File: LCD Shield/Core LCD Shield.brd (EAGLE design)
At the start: 38.1 x 35.6 mm, 8 parts, among them IC1 MC33269T-5.0, J1 TWIG_2.0-DIP-FEMALE

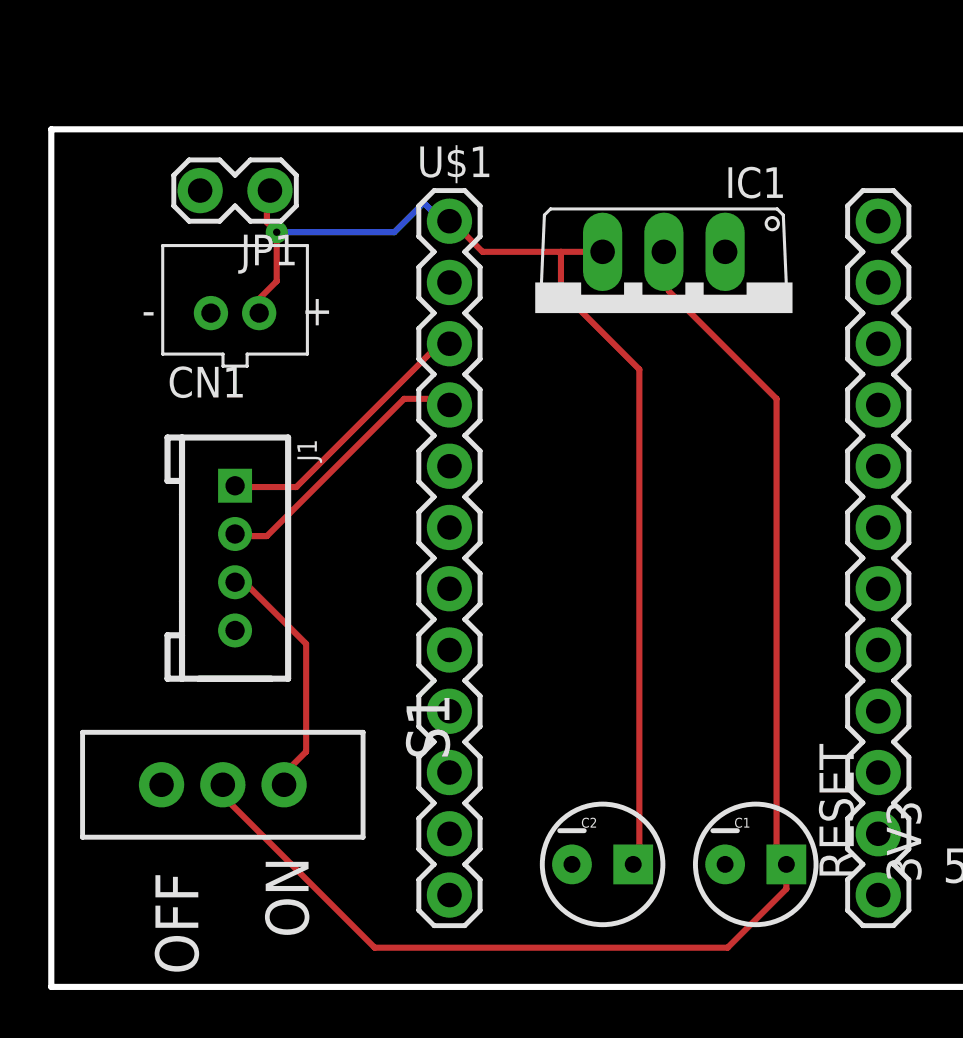
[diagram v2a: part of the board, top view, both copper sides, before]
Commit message: Reviewed LCD Shield
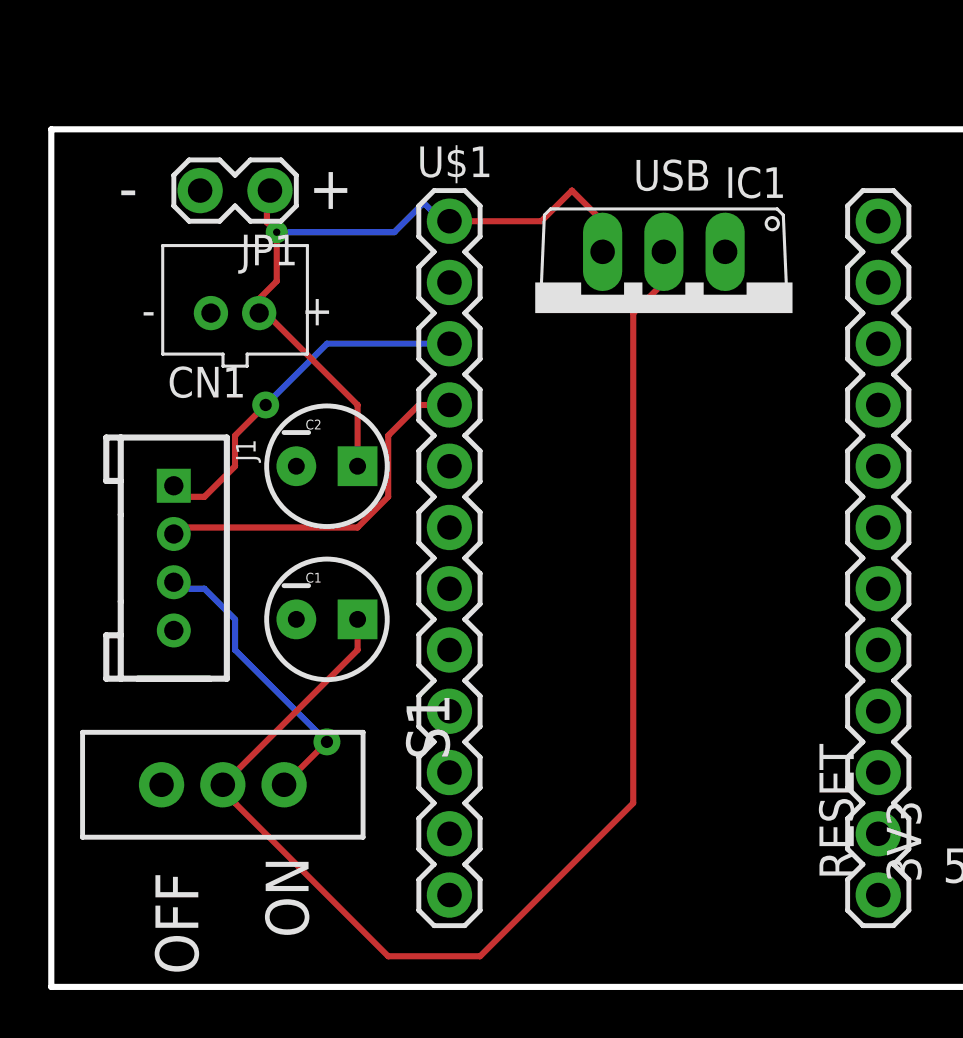
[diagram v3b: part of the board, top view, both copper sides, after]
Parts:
- added U$2: (no value), Spark:SPARK_LOGO
- moved C1 20.5 mm to (11.4, 15.2)
- moved C2 20.1 mm to (11.4, 21.6)
- moved J1 2.54 mm to (5.08, 17.8)
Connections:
- net +3V3 renamed VCC
- removed net RESET: U$1.23
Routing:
- net VIN: track 47.4 -> 30.6 mm
- net RX: track 11.4 -> 15.3 mm
- net TX: track 11.5 -> 15.3 mm, vias 0 -> 1
- net +5V: track 10.5 -> 12.5 mm, vias 0 -> 1
- net N1: track 56.1 -> 55.2 mm
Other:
- board text added: "+"
- board text added: "-"
- board text added: "Spark LCD Shield v0.1 2013-04-08"
- board text added: "USB"
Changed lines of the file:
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@@
 <wire x1="38.1" y1="35.56" x2="38.1" y2="0" width="0.254" layer="20"/>
 <wire x1="38.1" y1="0" x2="0" y2="0" width="0.254" layer="20"/>
+<text x="10.668" y="32.258" size="1.778" layer="21" font="vector" ratio="15">+</text>
+<text x="2.794" y="32.258" size="1.778" layer="21" font="vector" ratio="15">-</text>
+<text x="24.13" y="33.02" size="1.27" layer="21" font="vector" ratio="15">USB</text>
+<text x="22.86" y="2.54" size="1.27" layer="22" font="vector" ratio="15" rot="MR90">Spark LCD Shield
+v0.1
+2013-04-08</text>
 </plain>
 <attributes>
@@
 <element name="U$1" library="Spark" package="SPARK_CORE" value="SPARK_CORECORE" x="25.4" y="17.78"/>
 <element name="IC1" library="linear" package="TO220V" value="MC33269T-5.0" x="25.4" y="27.94" rot="R180"/>
-<element name="C1" library="SparkFun-Capacitors" package="CPOL-RADIAL-10UF-25V" value="10uF" x="29.21" y="5.08"/>
-<element name="C2" library="SparkFun-Capacitors" package="CPOL-RADIAL-10UF-25V" value="1uF" x="22.86" y="5.08"/>
+<element name="C1" library="SparkFun-Capacitors" package="CPOL-RADIAL-10UF-25V" value="10uF" x="11.43" y="15.24"/>
+<element name="C2" library="SparkFun-Capacitors" package="CPOL-RADIAL-10UF-25V" value="1uF" x="11.43" y="21.59"/>
 <element name="CN1" library="adafruit" package="JST-PH-2-THM" value="" x="7.62" y="27.94"/>
 <element name="JP1" library="SparkFun-Connectors" package="1X02_LOCK" value="" x="8.89" y="33.02" rot="R180"/>
 <element name="S1" library="SparkFun-Electromechanical" package="SWITCH-SPDT" value="" x="7.112" y="8.382" rot="R270"/>
-<element name="J1" library="Connector" package="2.0_1X4" value="TWIG_2.0-DIP-FEMALE" x="7.62" y="17.78" rot="R270"/>
+<element name="J1" library="Connector" package="2.0_1X4" value="TWIG_2.0-DIP-FEMALE" x="5.08" y="17.78" rot="R270"/>
+<element name="U$2" library="Spark" package="SPARK_LOGO" value="" x="22.86" y="2.54"/>
 </elements>
 <signals>
@@
 <contactref element="S1" pad="1"/>
 <contactref element="J1" pad="3"/>
-<wire x1="8.128" y1="16.6624" x2="7.7216" y2="16.6624" width="0.254" layer="1"/>
-<wire x1="10.5664" y1="14.224" x2="8.128" y2="16.6624" width="0.254" layer="1"/>
-<wire x1="10.5664" y1="9.7536" x2="10.5664" y2="14.224" width="0.254" layer="1"/>
-<wire x1="9.3472" y1="8.5344" x2="10.5664" y2="9.7536" width="0.254" layer="1"/>
-<wire x1="7.7216" y1="16.6624" x2="7.62" y2="16.78" width="0.254" layer="1"/>
-<wire x1="9.3472" y1="8.5344" x2="9.652" y2="8.382" width="0.254" layer="1"/>
+<wire x1="11.43" y1="10.16" x2="9.652" y2="8.382" width="0.254" layer="1"/>
+<wire x1="7.62" y1="13.97" x2="11.43" y2="10.16" width="0.254" layer="16"/>
+<wire x1="7.62" y1="15.24" x2="7.62" y2="13.97" width="0.254" layer="16"/>
+<wire x1="6.35" y1="16.51" x2="7.62" y2="15.24" width="0.254" layer="16"/>
+<wire x1="5.08" y1="16.51" x2="6.35" y2="16.51" width="0.254" layer="16"/>
+<wire x1="5.08" y1="16.51" x2="5.08" y2="16.78" width="0.254" layer="16"/>
+<via x="11.43" y="10.16" extent="1-16" drill="0.508"/>
 </signal>
 <signal name="GND">
@@
 </polygon>
 </signal>
-<signal name="RESET">
-<contactref element="U$1" pad="23"/>
-</signal>
 <signal name="VIN">
 <contactref element="U$1" pad="1"/>
@@
 <wire x1="8.5344" y1="28.0416" x2="8.62" y2="27.94" width="0.254" layer="1"/>
 <wire x1="8.9408" y1="32.9184" x2="9.0678" y2="33.02" width="0.254" layer="1"/>
-<wire x1="17.8816" y1="30.48" x2="21.1328" y2="30.48" width="0.254" layer="1"/>
-<wire x1="21.1328" y1="30.48" x2="22.86" y2="30.48" width="0.254" layer="1"/>
-<wire x1="16.6624" y1="31.6992" x2="17.8816" y2="30.48" width="0.254" layer="1"/>
-<wire x1="16.6624" y1="31.6992" x2="16.51" y2="31.75" width="0.254" layer="1"/>
-<wire x1="24.384" y1="25.6032" x2="24.384" y2="5.2832" width="0.254" layer="1"/>
-<wire x1="21.1328" y1="28.8544" x2="24.384" y2="25.6032" width="0.254" layer="1"/>
-<wire x1="21.1328" y1="30.48" x2="21.1328" y2="28.8544" width="0.254" layer="1"/>
-<wire x1="24.384" y1="5.2832" x2="24.13" y2="5.08" width="0.254" layer="1"/>
 <wire x1="14.224" y1="31.2928" x2="9.3472" y2="31.2928" width="0.254" layer="16"/>
 <wire x1="15.4432" y1="32.512" x2="14.224" y2="31.2928" width="0.254" layer="16"/>
@@
 <wire x1="16.256" y1="31.6992" x2="16.51" y2="31.75" width="0.254" layer="16"/>
 <via x="9.3472" y="31.2928" extent="1-16" drill="0.3048"/>
-</signal>
-<signal name="+3V3">
-<contactref element="U$1" pad="24"/>
+<wire x1="12.7" y1="24.13" x2="12.7" y2="21.59" width="0.254" layer="1"/>
+<wire x1="8.89" y1="27.94" x2="12.7" y2="24.13" width="0.254" layer="1"/>
+<wire x1="8.89" y1="27.94" x2="8.62" y2="27.94" width="0.254" layer="1"/>
+<wire x1="20.32" y1="31.75" x2="16.51" y2="31.75" width="0.254" layer="1"/>
+<wire x1="21.59" y1="33.02" x2="20.32" y2="31.75" width="0.254" layer="1"/>
+<wire x1="22.86" y1="31.75" x2="21.59" y2="33.02" width="0.254" layer="1"/>
+<wire x1="22.86" y1="30.48" x2="22.86" y2="31.75" width="0.254" layer="1"/>
 </signal>
 <signal name="N1">
@@
 <contactref element="C1" pad="1"/>
 <contactref element="S1" pad="2"/>
-<wire x1="25.6032" y1="28.8544" x2="25.6032" y2="30.48" width="0.254" layer="1"/>
-<wire x1="30.0736" y1="24.384" x2="25.6032" y2="28.8544" width="0.254" layer="1"/>
-<wire x1="30.0736" y1="5.6896" x2="30.0736" y2="24.384" width="0.254" layer="1"/>
-<wire x1="30.48" y1="5.2832" x2="30.0736" y2="5.6896" width="0.254" layer="1"/>
-<wire x1="25.6032" y1="30.48" x2="25.4" y2="30.48" width="0.254" layer="1"/>
-<wire x1="30.48" y1="5.2832" x2="30.48" y2="5.08" width="0.254" layer="1"/>
-<wire x1="7.3152" y1="7.7216" x2="7.3152" y2="8.128" width="0.254" layer="1"/>
-<wire x1="13.4112" y1="1.6256" x2="7.3152" y2="7.7216" width="0.254" layer="1"/>
-<wire x1="28.0416" y1="1.6256" x2="13.4112" y2="1.6256" width="0.254" layer="1"/>
-<wire x1="30.48" y1="4.064" x2="28.0416" y2="1.6256" width="0.254" layer="1"/>
-<wire x1="30.48" y1="5.08" x2="30.48" y2="4.064" width="0.254" layer="1"/>
-<wire x1="7.3152" y1="8.128" x2="7.112" y2="8.382" width="0.254" layer="1"/>
+<wire x1="12.7" y1="13.97" x2="7.112" y2="8.382" width="0.254" layer="1"/>
+<wire x1="12.7" y1="15.24" x2="12.7" y2="13.97" width="0.254" layer="1"/>
+<wire x1="13.97" y1="1.27" x2="7.62" y2="7.62" width="0.254" layer="1"/>
+<wire x1="17.78" y1="1.27" x2="13.97" y2="1.27" width="0.254" layer="1"/>
+<wire x1="24.13" y1="7.62" x2="17.78" y2="1.27" width="0.254" layer="1"/>
+<wire x1="24.13" y1="27.94" x2="24.13" y2="7.62" width="0.254" layer="1"/>
+<wire x1="25.4" y1="29.21" x2="24.13" y2="27.94" width="0.254" layer="1"/>
+<wire x1="25.4" y1="30.48" x2="25.4" y2="29.21" width="0.254" layer="1"/>
+<wire x1="7.62" y1="7.62" x2="7.112" y2="8.382" width="0.254" layer="1"/>
 </signal>
 <signal name="VDDA">
@@
 <contactref element="J1" pad="2"/>
 <contactref element="U$1" pad="4"/>
-<wire x1="8.9408" y1="18.6944" x2="7.7216" y2="18.6944" width="0.254" layer="1"/>
-<wire x1="14.6304" y1="24.384" x2="8.9408" y2="18.6944" width="0.254" layer="1"/>
-<wire x1="16.256" y1="24.384" x2="14.6304" y2="24.384" width="0.254" layer="1"/>
-<wire x1="7.7216" y1="18.6944" x2="7.62" y2="18.78" width="0.254" layer="1"/>
-<wire x1="16.256" y1="24.384" x2="16.51" y2="24.13" width="0.254" layer="1"/>
+<wire x1="5.08" y1="19.05" x2="12.7" y2="19.05" width="0.254" layer="1"/>
+<wire x1="5.08" y1="19.05" x2="5.08" y2="18.78" width="0.254" layer="1"/>
+<wire x1="13.97" y1="20.32" x2="12.7" y2="19.05" width="0.254" layer="1"/>
+<wire x1="13.97" y1="22.86" x2="13.97" y2="20.32" width="0.254" layer="1"/>
+<wire x1="15.24" y1="24.13" x2="13.97" y2="22.86" width="0.254" layer="1"/>
+<wire x1="16.51" y1="24.13" x2="15.24" y2="24.13" width="0.254" layer="1"/>
 </signal>
 <signal name="TX">
 <contactref element="J1" pad="1"/>
 <contactref element="U$1" pad="3"/>
-<wire x1="10.16" y1="20.7264" x2="7.7216" y2="20.7264" width="0.254" layer="1"/>
-<wire x1="16.256" y1="26.8224" x2="10.16" y2="20.7264" width="0.254" layer="1"/>
-<wire x1="7.7216" y1="20.7264" x2="7.62" y2="20.78" width="0.254" layer="1"/>
-<wire x1="16.256" y1="26.8224" x2="16.51" y2="26.67" width="0.254" layer="1"/>
+<wire x1="5.08" y1="20.32" x2="6.35" y2="20.32" width="0.254" layer="1"/>
+<wire x1="5.08" y1="20.32" x2="5.08" y2="20.78" width="0.254" layer="1"/>
+<wire x1="7.62" y1="21.59" x2="6.35" y2="20.32" width="0.254" layer="1"/>
+<wire x1="7.62" y1="22.86" x2="7.62" y2="21.59" width="0.254" layer="1"/>
+<wire x1="8.89" y1="24.13" x2="7.62" y2="22.86" width="0.254" layer="1"/>
+<wire x1="11.43" y1="26.67" x2="8.89" y2="24.13" width="0.254" layer="16"/>
+<wire x1="16.51" y1="26.67" x2="11.43" y2="26.67" width="0.254" layer="16"/>
+<via x="8.89" y="24.13" extent="1-16" drill="0.508"/>
+</signal>
+<signal name="VCC">
+<contactref element="U$1" pad="24"/>
 </signal>
 </signals>
 </board>
 </drawing>
+<compatibility>
+<note version="6.3" minversion="6.2.2" severity="warning">
+Since Version 6.2.2 text objects can contain more than one line,
+which will not be processed correctly with this version.
+</note>
+</compatibility>
 </eagle>
